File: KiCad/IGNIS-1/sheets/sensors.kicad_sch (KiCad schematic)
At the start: 9 parts, among them U20 BME280, U21 MPU6050, U22 MQ-135, U24 GPS NEO-6M

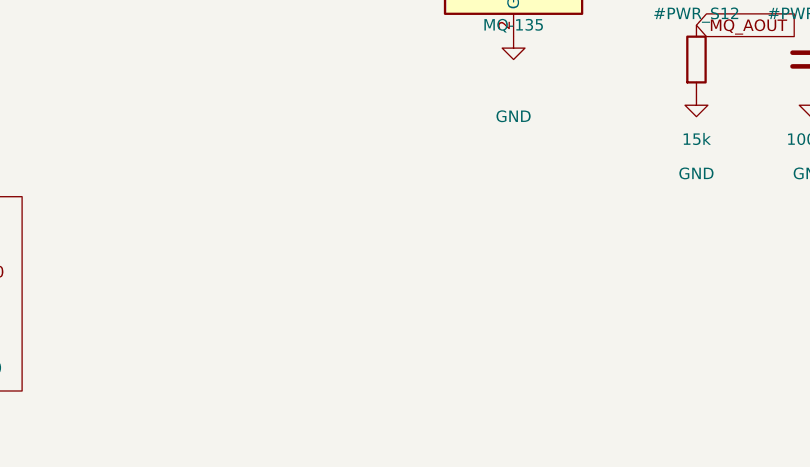
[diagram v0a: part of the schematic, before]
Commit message: Actualizado los boards de IGNIS - separado en 3 boards
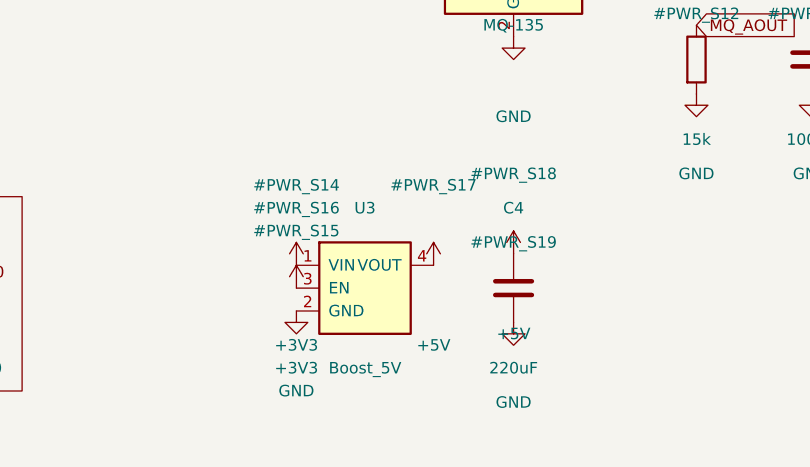
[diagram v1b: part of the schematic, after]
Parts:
- added C4: 220uF, Capacitor_SMD:C_1210_3225Metric, symbol Device:C
- added U3: Boost_5V, Connector_PinHeader_2.54mm:PinHeader_1x04_P2.54mm_Vertical, symbol IGNIS1:DCDC_Module
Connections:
- net +3V3: now also U3.1 (VIN), U3.3 (EN)
- net +5V: now also C4.1, U3.4 (VOUT)
- net GND: now also C4.2, U3.2 (GND)
